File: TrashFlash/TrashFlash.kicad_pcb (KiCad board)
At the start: 6 copper layers, 108 x 60 mm, 154 parts, among them IC201 AD8615AUJZ-REEL, IC202 ADG5419BCPZ-RL7, IC203 SN74LXC2T45QDTTRQ1, IC301 LTC3643IUDD#PBF, IC401 STM32L471QEI6, IC501 TPS63900DSKR, IC502 TPS63900DSKR, IC601 LP5024RSMR, IC602 PEC11S-929K-S0015, IC701 BQ27426YZFR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

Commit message: LED via stitch und han gmerkt das ich usversehe d batterie im letschte kommit use gno han sorry :)
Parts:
- Q201, Q202, Q203, Q204: moved to B.Cu
- moved Q204 65.7 mm to (135.0, 115.0), turned to 180 degrees
- moved Q203 57.1 mm to (131.0, 115.0), turned to 180 degrees
- moved Q202 48.5 mm to (127.0, 115.0), turned to 180 degrees
- moved Q201 40.2 mm to (123.0, 115.0), turned to 180 degrees
- moved C306 4.53 mm to (105.5, 117.8)
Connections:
- net /SELECT_VDD renamed /SELECT_VDD_1
- D201 pad TP: unconnected-(D201-PadTP) -> /LED_Current_Source/LED_TP
- D202 pad TP: unconnected-(D202-PadTP) -> /LED_Current_Source/LED_TP
- D203 pad TP: unconnected-(D203-PadTP) -> /LED_Current_Source/LED_TP
- D204 pad TP: unconnected-(D204-PadTP) -> /LED_Current_Source/LED_TP
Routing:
- net /LED_Current_Source/LED_TP: vias 0 -> 386
- net (no net): vias 0 -> 1

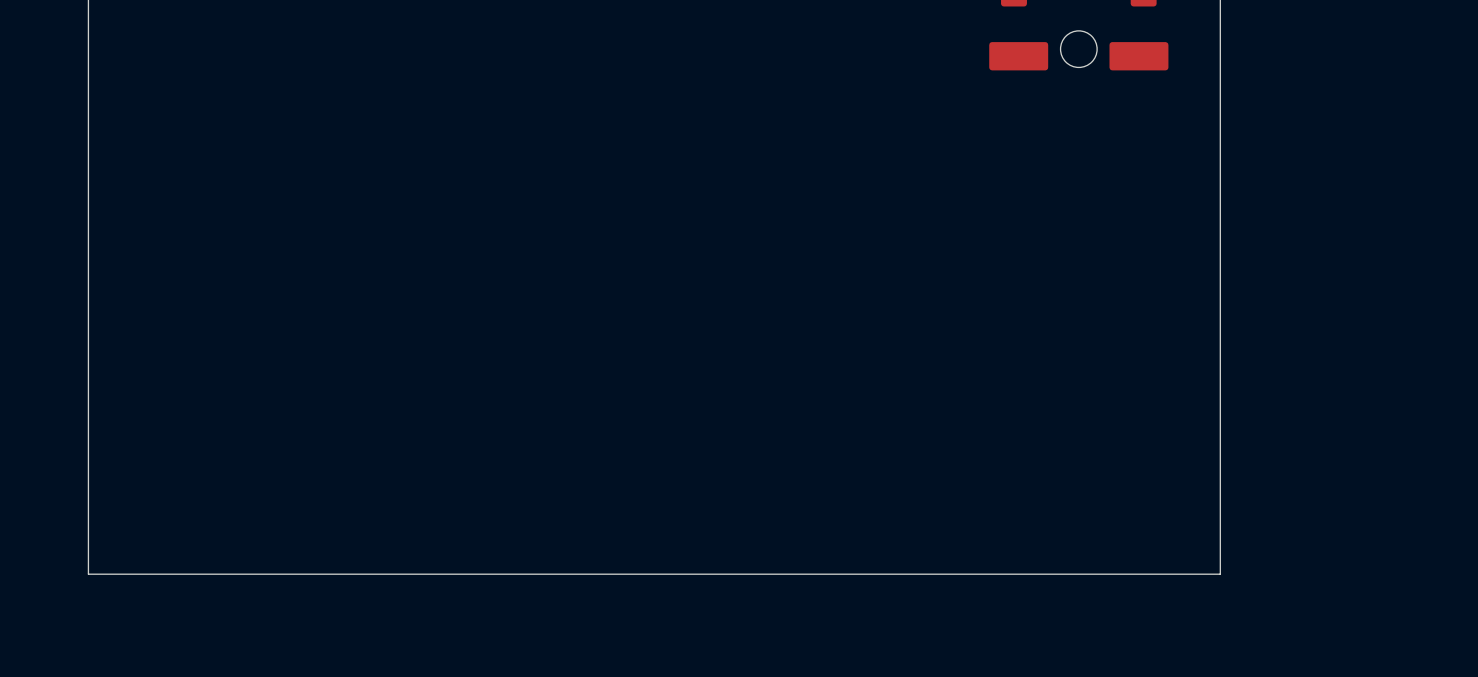
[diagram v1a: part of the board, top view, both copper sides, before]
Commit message: Added battery and connectors, Schematic remark for BQ297xx
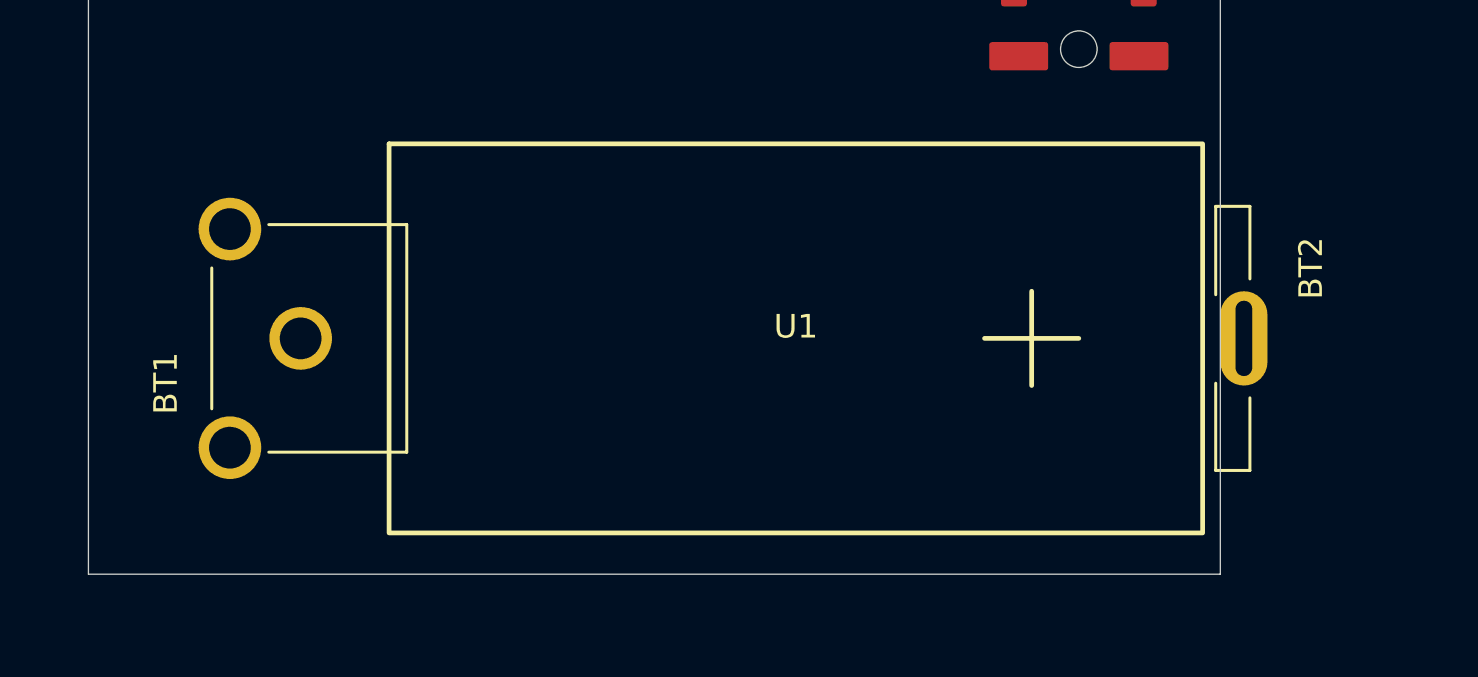
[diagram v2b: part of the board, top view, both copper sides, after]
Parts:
- added BT1: 628, TrashFlash:BAT_628, F.Cu at (109.0, 150.0)
- added BT2: 5223, TrashFlash:BAT_5223, F.Cu at (149.0, 150.0)
- added U1: ~, TrashFlash:CR123A, F.Cu at (130.0, 150.0)

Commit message: Some layout suggestions
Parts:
- C406, C407, C408, C409, C410, C411, C412, C413, C414, IC601, J701, R709, R710: moved to B.Cu
- moved J103 92.6 mm to (259.8, 102.8)
- moved R709 88.6 mm to (170.0, 104.8), turned to 90 degrees
- moved R710 87.8 mm to (170.0, 108.8), turned to -90 degrees
- moved J701 87.6 mm to (163.8, 107.0), turned to 90 degrees
- moved C601 48.5 mm to (278.7, 134.0)
- moved C602 48.5 mm to (278.7, 130.5)
- moved R601 48.5 mm to (274.2, 134.2)
- moved R602 48.5 mm to (274.2, 131.5)
- moved R603 48.5 mm to (274.2, 129.0)
- moved IC601 44.3 mm to (191.0, 127.0), turned to 180 degrees
- moved IC401 36.9 mm to (256.0, 121.2)
- moved C408 31.3 mm to (258.2, 120.0), turned to -90 degrees
- moved C407 29.7 mm to (254.3, 119.5), turned to 180 degrees
- moved R401 29.0 mm to (264.0, 122.5)
- moved R402 29.0 mm to (264.0, 120.0)
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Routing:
- net +5V: track 0.00 -> 13.6 mm
- net VDD: track 0.00 -> 0.50 mm, vias 0 -> 4
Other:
- board text added: "Silkscreen min: Change all labels Tickness: 0.15 Height: 1mm"
